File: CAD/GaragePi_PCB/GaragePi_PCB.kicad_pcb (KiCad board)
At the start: 2 copper layers, 13 parts, among them J1 Screw_Terminal_01x03, J2 Screw_Terminal_01x03, J3 Raspberry_Pi_2_3, J4 Screw_Terminal_01x03, J5 Screw_Terminal_01x03, K1 SANYOU_SRD_Form_C, K2 SANYOU_SRD_Form_C, Q1 PN2222A, Q2 PN2222A

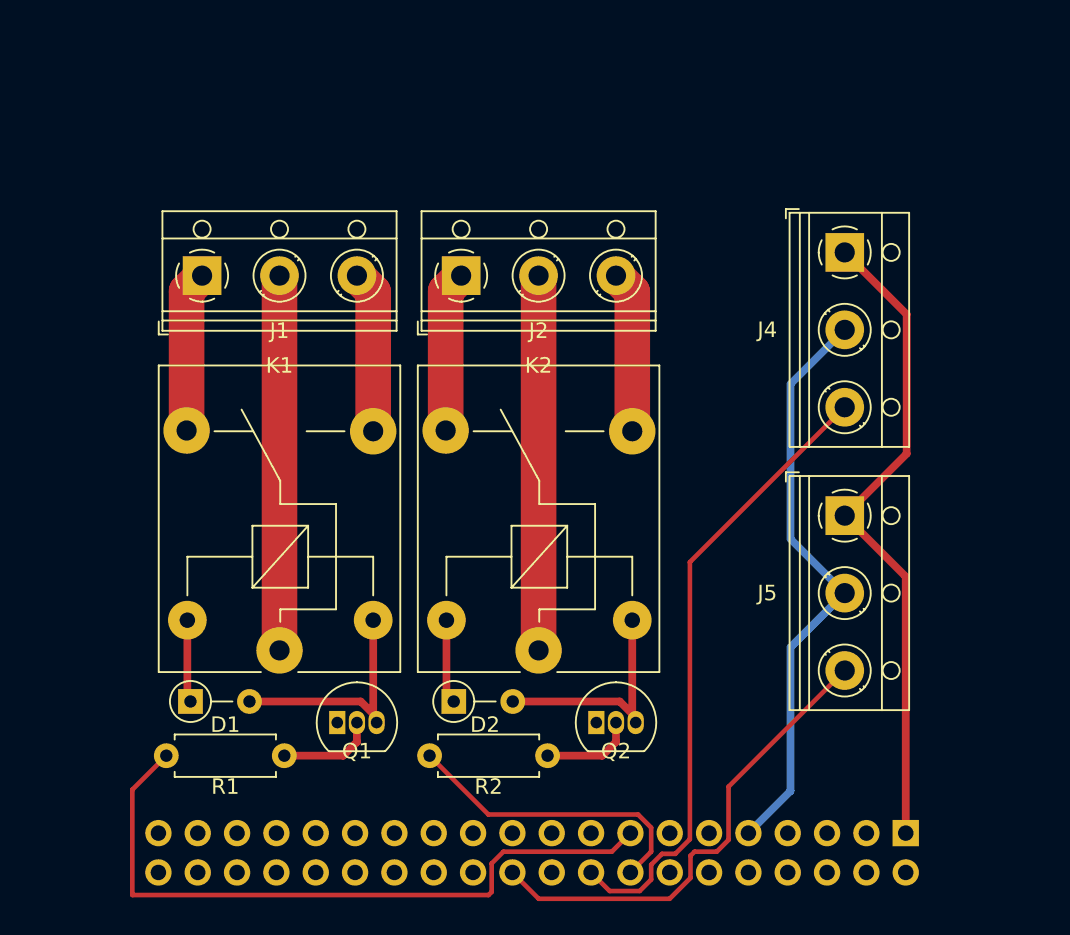
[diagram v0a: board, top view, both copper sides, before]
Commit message: completed PCB schematics v0.1; Updated README with the project update
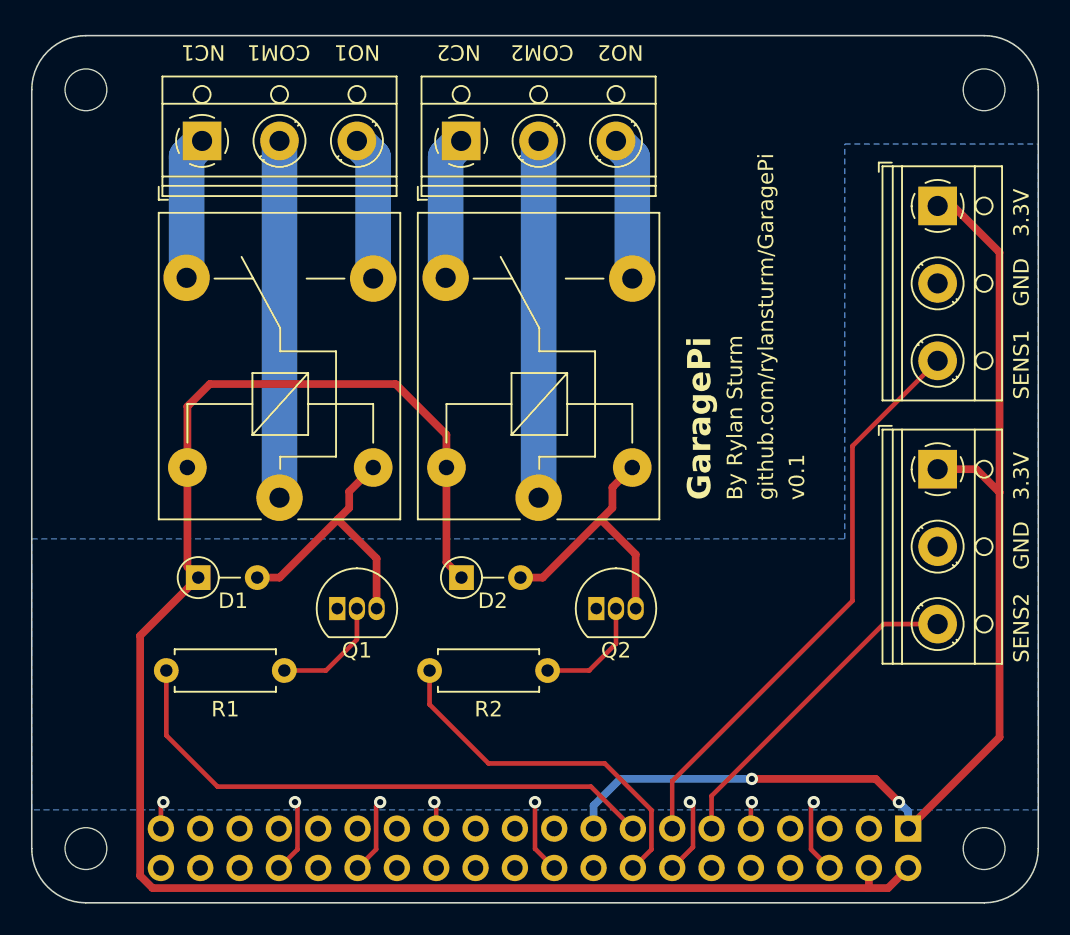
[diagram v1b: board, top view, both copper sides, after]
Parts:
- added H1: MountingHole, MountingHole:MountingHole_2.7mm_M2.5, F.Cu at (159.0, 48.0)
- added H2: MountingHole, MountingHole:MountingHole_2.7mm_M2.5, F.Cu at (101.0, 48.0)
- added H3: MountingHole, MountingHole:MountingHole_2.7mm_M2.5, F.Cu at (159.0, 97.0)
- added H4: MountingHole, MountingHole:MountingHole_2.7mm_M2.5, F.Cu at (101.0, 97.0)
- moved K1 9.86 mm to (113.5, 74.3)
- moved K2 9.86 mm to (130.2, 74.3)
- moved J1 8.70 mm to (108.5, 51.3)
- moved J2 8.70 mm to (125.2, 51.3)
- moved D1 8.02 mm to (108.3, 79.5)
- moved D2 8.02 mm to (125.3, 79.5)
- moved Q1 7.36 mm to (117.2, 81.5)
- moved Q2 7.36 mm to (134.0, 81.5)
- moved J4 6.71 mm to (156.0, 55.5)
- moved J5 6.71 mm to (156.0, 72.5)
- moved R1 5.50 mm to (113.8, 85.5)
- moved R2 5.50 mm to (130.8, 85.5)
- moved J3 0.33 mm to (154.1, 95.7)
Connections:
- J3 pad 11: unconnected-(J3-GPIO17-Pad11) -> /SENSOR_2
- J3 pad 13: unconnected-(J3-GPIO27-Pad13) -> /SENSOR_1
- J3 pad 18: /SENSOR_1 -> unconnected-(J3-GPIO24-Pad18)
- J3 pad 22: /SENSOR_2 -> unconnected-(J3-GPIO25-Pad22)
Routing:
- net +5V: track 10.8 -> 112.2 mm
- net +3.3V: track 42.4 -> 74.0 mm, vias 0 -> 2
- net /SENSOR_2: track 31.1 -> 21.3 mm
- net GND: track 38.0 -> 29.4 mm, vias 0 -> 8
- net /RELAY_1: track 44.8 -> 36.8 mm
- net /RELAY_2: track 19.7 -> 23.6 mm
- net /SENSOR_1: track 40.9 -> 37.3 mm
- net Net-(D2-A): track 15.4 -> 17.5 mm
- net Net-(Q2-B): track 6.04 -> 7.55 mm
- net Net-(D1-A): track 16.6 -> 17.8 mm
- net Net-(Q1-B): track 6.31 -> 7.52 mm
- net Net-(J1-Pin_3): track 10.5 -> 9.32 mm
- net Net-(J2-Pin_3): track 10.5 -> 9.32 mm
- net Net-(J2-Pin_2): track 24.2 -> 23.0 mm
- net Net-(J2-Pin_1): track 10.4 -> 9.25 mm
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- added copper zone on B.Cu, net GND
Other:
- board outline added: 65 x 56 mm
- board text added: "3.3V"
- board text added: "By Rylan Sturm"
- board text added: "COM1"
- board text added: "COM2"
- board text added: "GND"
- board text added: "GaragePi"
- board text added: "NC1"
- board text added: "NC2"
- board text added: "NO1"
- board text added: "NO2"
- board text added: "SENS1"
- board text added: "SENS2"
- board text added: "github.com/rylansturm/GaragePi"
- board text added: "v0.1"
